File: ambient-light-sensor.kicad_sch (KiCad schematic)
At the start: 5 parts, among them Q1 TEPT4400

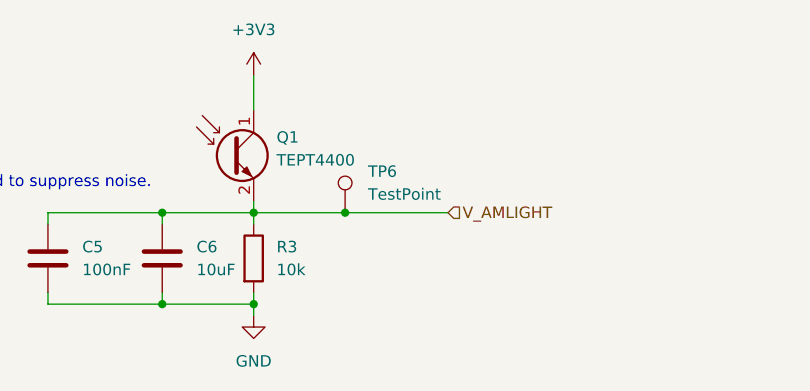
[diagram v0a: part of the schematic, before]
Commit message: Place opto couplers and some connectors.
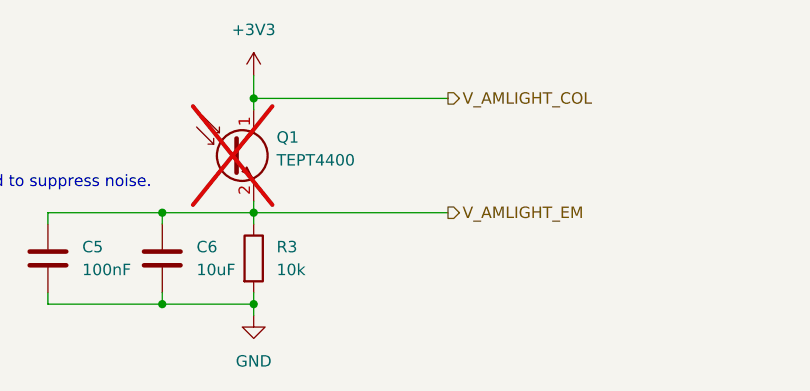
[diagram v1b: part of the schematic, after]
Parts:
- removed TP6: TestPoint, TestPoint:TestPoint_Pad_D1.0mm, symbol Connector:TestPoint
- Q1: now not fitted
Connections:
- net V_AMLIGHT renamed V_AMLIGHT_EM
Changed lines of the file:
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@@
 	)
 	(junction
-		(at 135.89 110.49)
+		(at 125.73 97.79)
 		(diameter 0)
 		(color 0 0 0 0)
@@
 	(wire
 		(pts
-			(xy 125.73 120.65) (xy 125.73 121.92)
+			(xy 125.73 97.79) (xy 125.73 99.06)
 		)
 		(stroke
@@
 	(wire
 		(pts
-			(xy 102.87 110.49) (xy 102.87 111.76)
+			(xy 125.73 120.65) (xy 125.73 121.92)
 		)
 		(stroke
@@
 	(wire
 		(pts
-			(xy 102.87 110.49) (xy 115.57 110.49)
+			(xy 102.87 110.49) (xy 102.87 111.76)
 		)
 		(stroke
@@
 	(wire
 		(pts
-			(xy 125.73 110.49) (xy 125.73 111.76)
+			(xy 102.87 110.49) (xy 115.57 110.49)
 		)
 		(stroke
@@
 	(wire
 		(pts
-			(xy 125.73 110.49) (xy 135.89 110.49)
+			(xy 125.73 110.49) (xy 125.73 111.76)
 		)
 		(stroke
@@
 	(wire
 		(pts
-			(xy 125.73 95.25) (xy 125.73 99.06)
+			(xy 125.73 110.49) (xy 147.32 110.49)
 		)
 		(stroke
@@
 	(wire
 		(pts
-			(xy 102.87 120.65) (xy 115.57 120.65)
+			(xy 125.73 95.25) (xy 125.73 97.79)
 		)
 		(stroke
@@
 	(wire
 		(pts
-			(xy 115.57 120.65) (xy 125.73 120.65)
+			(xy 102.87 120.65) (xy 115.57 120.65)
 		)
 		(stroke
@@
 	(wire
 		(pts
-			(xy 115.57 119.38) (xy 115.57 120.65)
+			(xy 115.57 120.65) (xy 125.73 120.65)
 		)
 		(stroke
@@
 	(wire
 		(pts
-			(xy 125.73 119.38) (xy 125.73 120.65)
+			(xy 125.73 97.79) (xy 147.32 97.79)
 		)
 		(stroke
@@
 	(wire
 		(pts
-			(xy 115.57 110.49) (xy 115.57 111.76)
+			(xy 115.57 119.38) (xy 115.57 120.65)
 		)
 		(stroke
@@
 	(wire
 		(pts
-			(xy 115.57 110.49) (xy 125.73 110.49)
+			(xy 125.73 119.38) (xy 125.73 120.65)
 		)
 		(stroke
@@
 	(wire
 		(pts
-			(xy 135.89 110.49) (xy 147.32 110.49)
+			(xy 115.57 110.49) (xy 115.57 111.76)
+		)
+		(stroke
+			(width 0)
+			(type default)
+		)
+	)
+	(wire
+		(pts
+			(xy 115.57 110.49) (xy 125.73 110.49)
 		)
 		(stroke
@@
 		)
 	)
-	(hierarchical_label "V_AMLIGHT"
-		(shape input)
+	(hierarchical_label "V_AMLIGHT_COL"
+		(shape output)
+		(at 147.32 97.79 0)
+		(effects
+			(font
+				(size 1.27 1.27)
+			)
+			(justify left)
+		)
+	)
+	(hierarchical_label "V_AMLIGHT_EM"
+		(shape output)
 		(at 147.32 110.49 0)
 		(effects
@@
 	)
 	(symbol
-		(lib_id "Connector:TestPoint")
-		(at 135.89 110.49 0)
-		(unit 1)
-		(exclude_from_sim no)
-		(in_bom yes)
-		(on_board yes)
-		(dnp no)
-		(fields_autoplaced yes)
-		(property "Reference" "TP6"
-			(at 138.43 105.9179 0)
-			(effects
-				(font
-					(size 1.27 1.27)
-				)
-				(justify left)
-			)
-		)
-		(property "Value" "TestPoint"
-			(at 138.43 108.4579 0)
-			(effects
-				(font
-					(size 1.27 1.27)
-				)
-				(justify left)
-			)
-		)
-		(property "Footprint" "TestPoint:TestPoint_Pad_D1.0mm"
-			(at 140.97 110.49 0)
-			(effects
-				(font
-					(size 1.27 1.27)
-				)
-				(hide yes)
-			)
-		)
-		(property "Datasheet" "~"
-			(at 140.97 110.49 0)
-			(effects
-				(font
-					(size 1.27 1.27)
-				)
-				(hide yes)
-			)
-		)
-		(property "Description" "test point"
-			(at 135.89 110.49 0)
-			(effects
-				(font
-					(size 1.27 1.27)
-				)
-				(hide yes)
-			)
-		)
-		(pin "1"
-		)
-		(instances
-			(project "stopnu-hardware"
-				(path "/4ab90003-ea4c-4878-8117-f834ac24f8d9/7b0869a3-a922-42ed-84a7-59d61dea9664"
-					(reference "TP6")
-					(unit 1)
-				)
-			)
-		)
-	)
-	(symbol
 		(lib_id "Device:R")
 		(at 125.73 115.57 0)
@@
 		(exclude_from_sim no)
 		(in_bom yes)
-		(on_board yes)
-		(dnp no)
+		(on_board no)
+		(dnp yes)
 		(fields_autoplaced yes)
 		(property "Reference" "Q1"

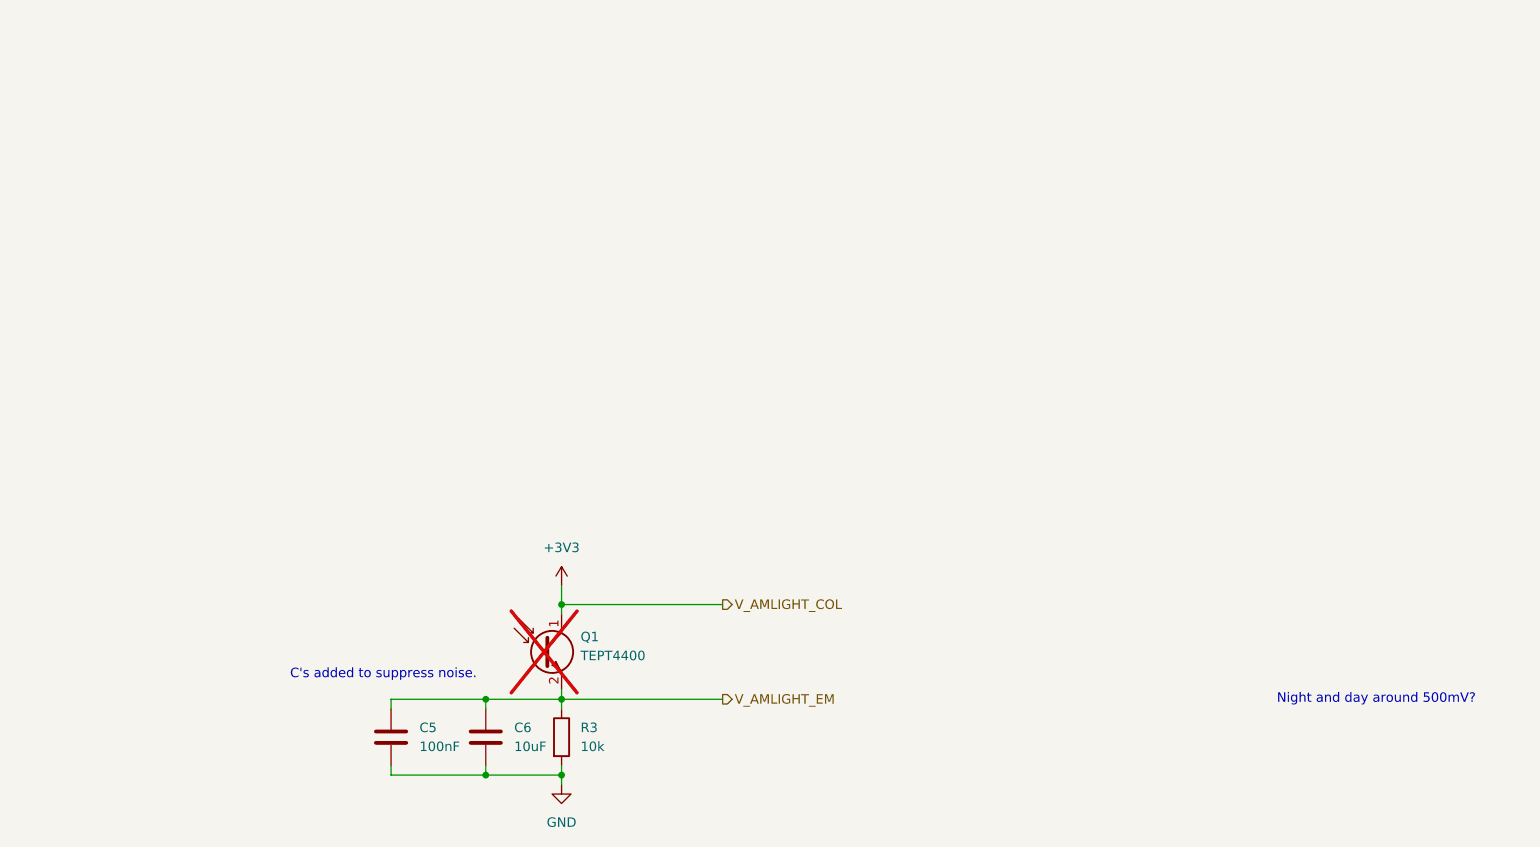
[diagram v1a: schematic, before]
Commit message: Labeled expansion port, fixed en pin U19 (high)
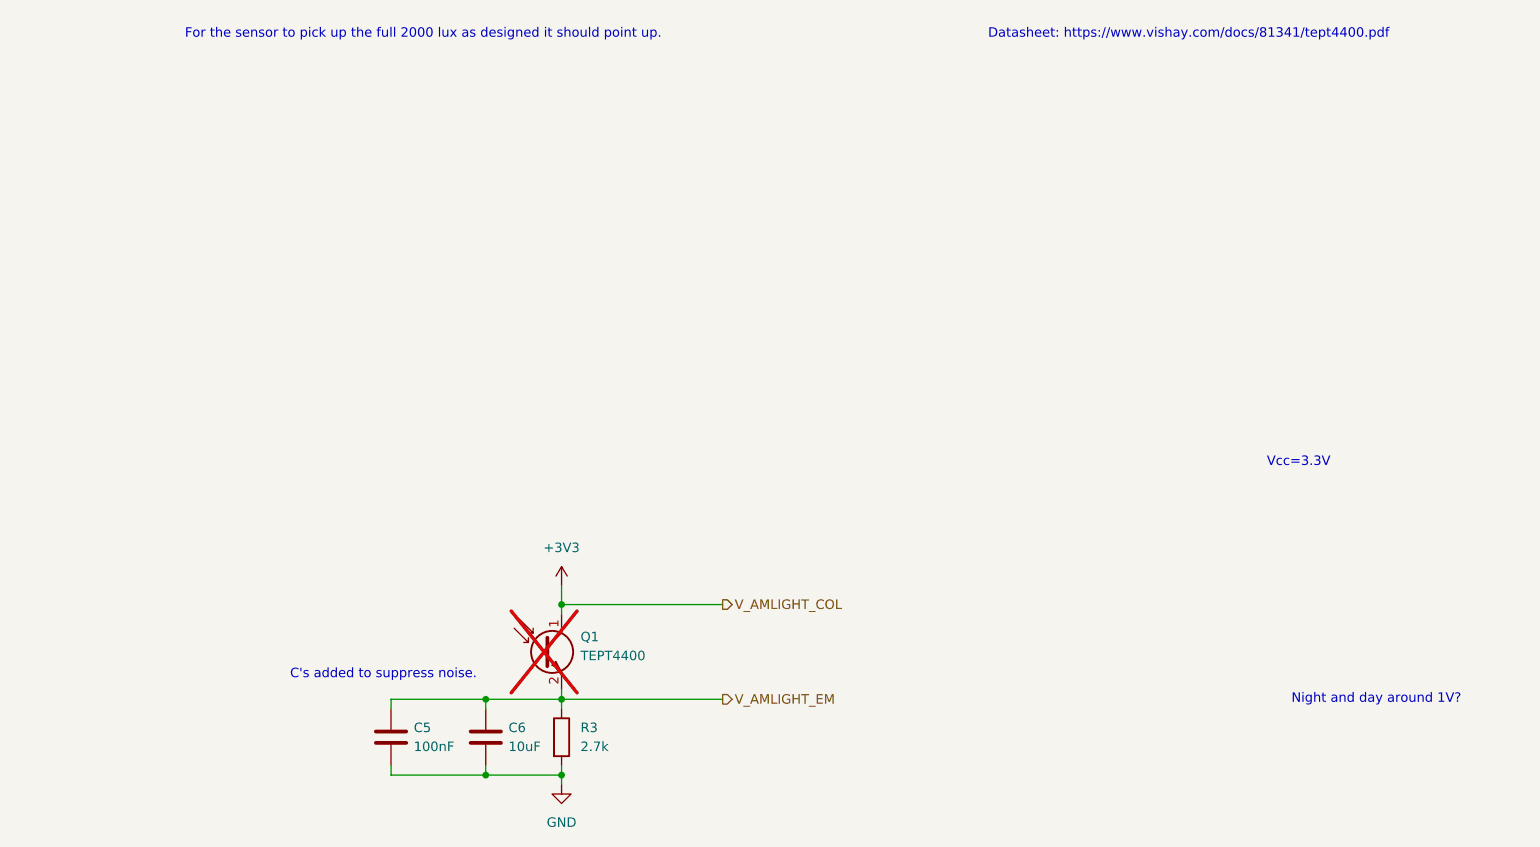
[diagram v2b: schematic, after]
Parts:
- R3: value 10k -> 2.7k; LCSC C25744 -> C13167
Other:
- note added: "Datasheet: https://www.vishay.com/docs/81341/tept4400.pdf"
- note added: "For the sensor to pick up the full 2000 lux as designed it should point up."
- note added: "Night and day around 1V?"
- note added: "Vcc=3.3V"
- note removed: "Night and day around 500mV?"

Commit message: Changed ambient light sensor to pull-up design.
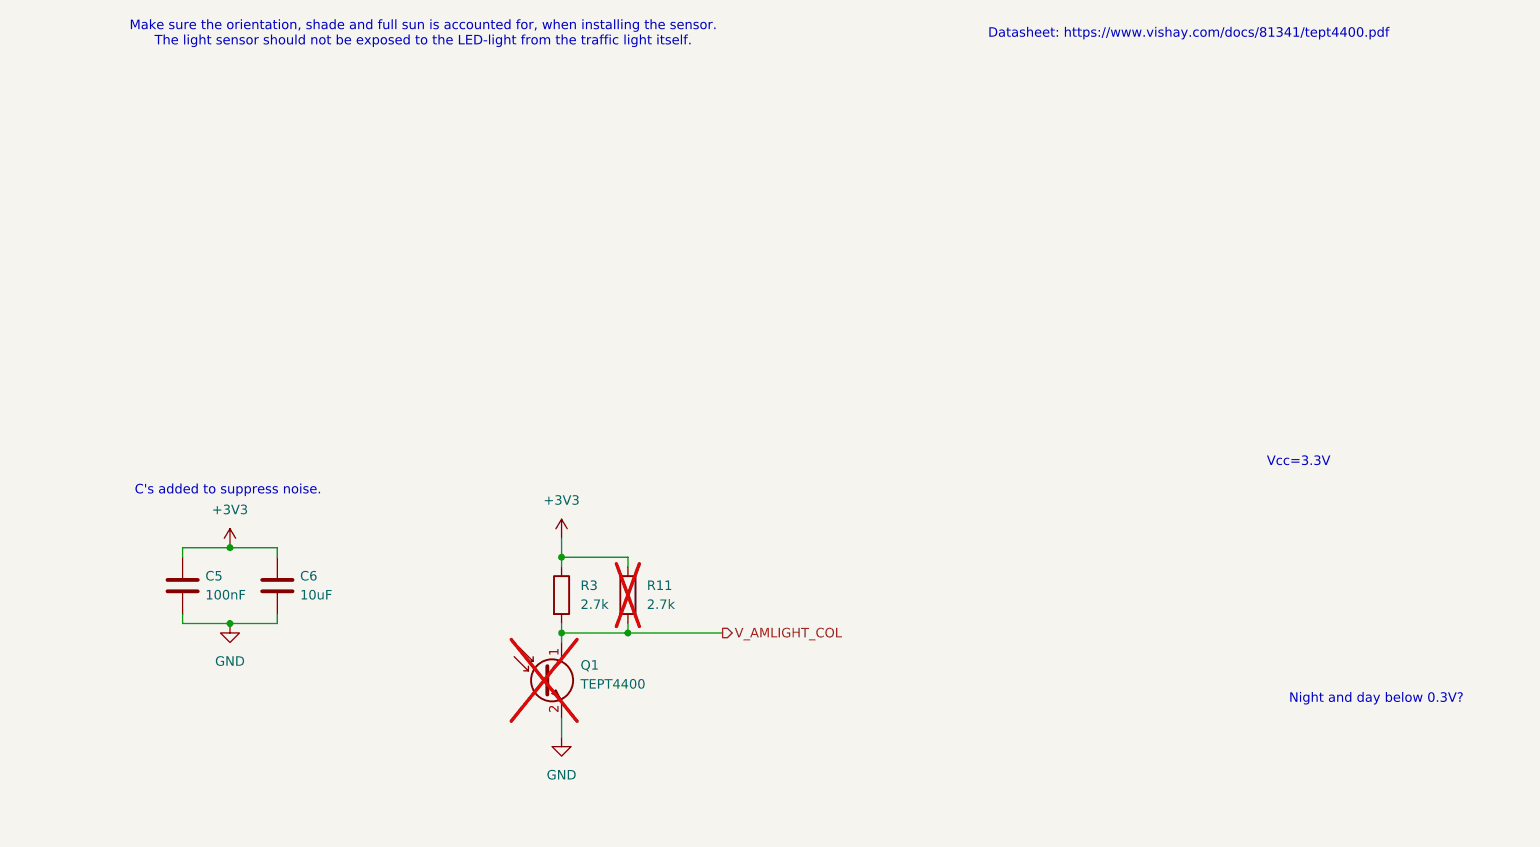
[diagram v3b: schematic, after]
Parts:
- added R11: 2.7k, Resistor_SMD:R_0603_1608Metric, symbol Device:R
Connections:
- net +3V3: now also C5.1, C6.1, R3.1, R11.1; no longer Q1.1 (C)
- net GND: now also Q1.2 (E); no longer R3.2
- removed net V_AMLIGHT_EM: C5.1, C6.1, Q1.2 (E), R3.1
- new net V_AMLIGHT_COL: Q1.1 (C), R11.2, R3.2
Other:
- note added: "Make sure the orientation, shade and full sun is accounted for, when installing the sensor. The light sensor should not be exposed to the LED-light from the traffic light itself."
- note added: "Night and day below 0.3V?"
- note removed: "For the sensor to pick up the full 2000 lux as designed it should point up."
- note removed: "Night and day around 1V?"
- moved on the sheet: C5, C6, Q1, R3
